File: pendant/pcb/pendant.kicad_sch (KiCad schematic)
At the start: 59 parts, among them CN1 S2B-PH-SM4-TB(LF)(SN), CN2 S4B-PH-SM4-TB(LF)(SN), Q1 DMG3415U-7, SW1 TS-1088-AR02016, SW2 TS-1088-AR02016, U1 ESP32-S3-WROOM-1, U2 TCA8418RTWR, U3 TPS61169DCKR, U5 APX803S-26SA-7, U6 MCP73831T-2ACI/OT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

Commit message: fix errors on pendant pcb
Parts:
- R5: footprint pendant:R0603 -> pendant:R0402; LCSC Part C365454 -> C203098
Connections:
- net DN1 is gone; now on net D-: D3.2, USBC1.A7 (DN1), USBC1.B7 (DN2)
- net VBUSD is gone; now on net VBUS: D4.2, USBC1.A4 (VBUS), USBC1.A9 (VBUS), USBC1.B4 (VBUS), USBC1.B9 (VBUS)
- net 3V3: now also C2.2, L1.2, U3.5 (VIN)
- net AXIS_X: now also U2.12 (COL3); no longer U2.13 (COL4)
- net AXIS_Y: now also U2.13 (COL4); no longer U2.14 (COL5)
- net AXIS_Z: now also U2.14 (COL5); no longer U2.15 (COL6)
- net D+: now also USBC1.A6 (DP1), USBC1.B6 (DP2)
- net D-: no longer D3.1
- net GND: now also D3.1, D4.1, D5.2, U2.19 (GND)
- net SPEED_1: now also U2.15 (COL6); no longer U2.16 (COL7)
- net SPEED_2: now also U2.16 (COL7); no longer U2.17 (COL8)
- net SPEED_3: now also U2.17 (COL8); no longer U2.18 (COL9)
- net SPEED_4: now also U2.18 (COL9); no longer U2.19 (GND)
- net VBUS: no longer C2.2, D4.1, L1.2, U3.5 (VIN)
- removed net DP1: D5.2, USBC1.A6 (DP1), USBC1.B6 (DP2)
- no-connect marks 66 -> 65
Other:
- moved on the sheet: R16

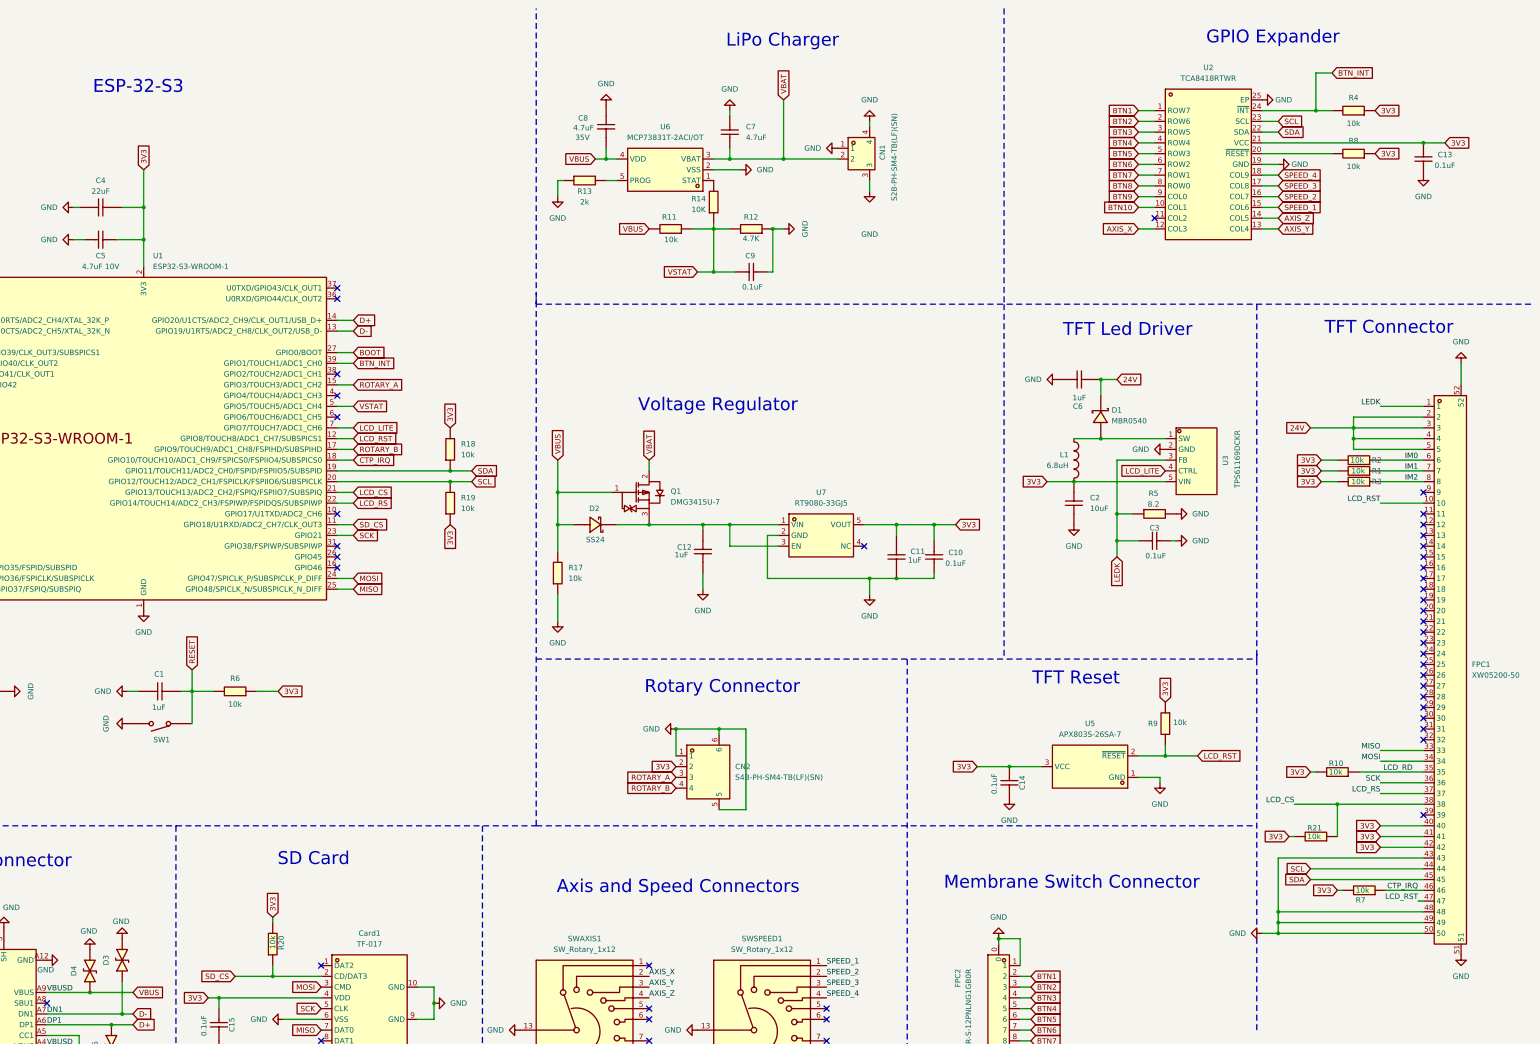
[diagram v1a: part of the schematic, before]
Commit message: update pendant pcb
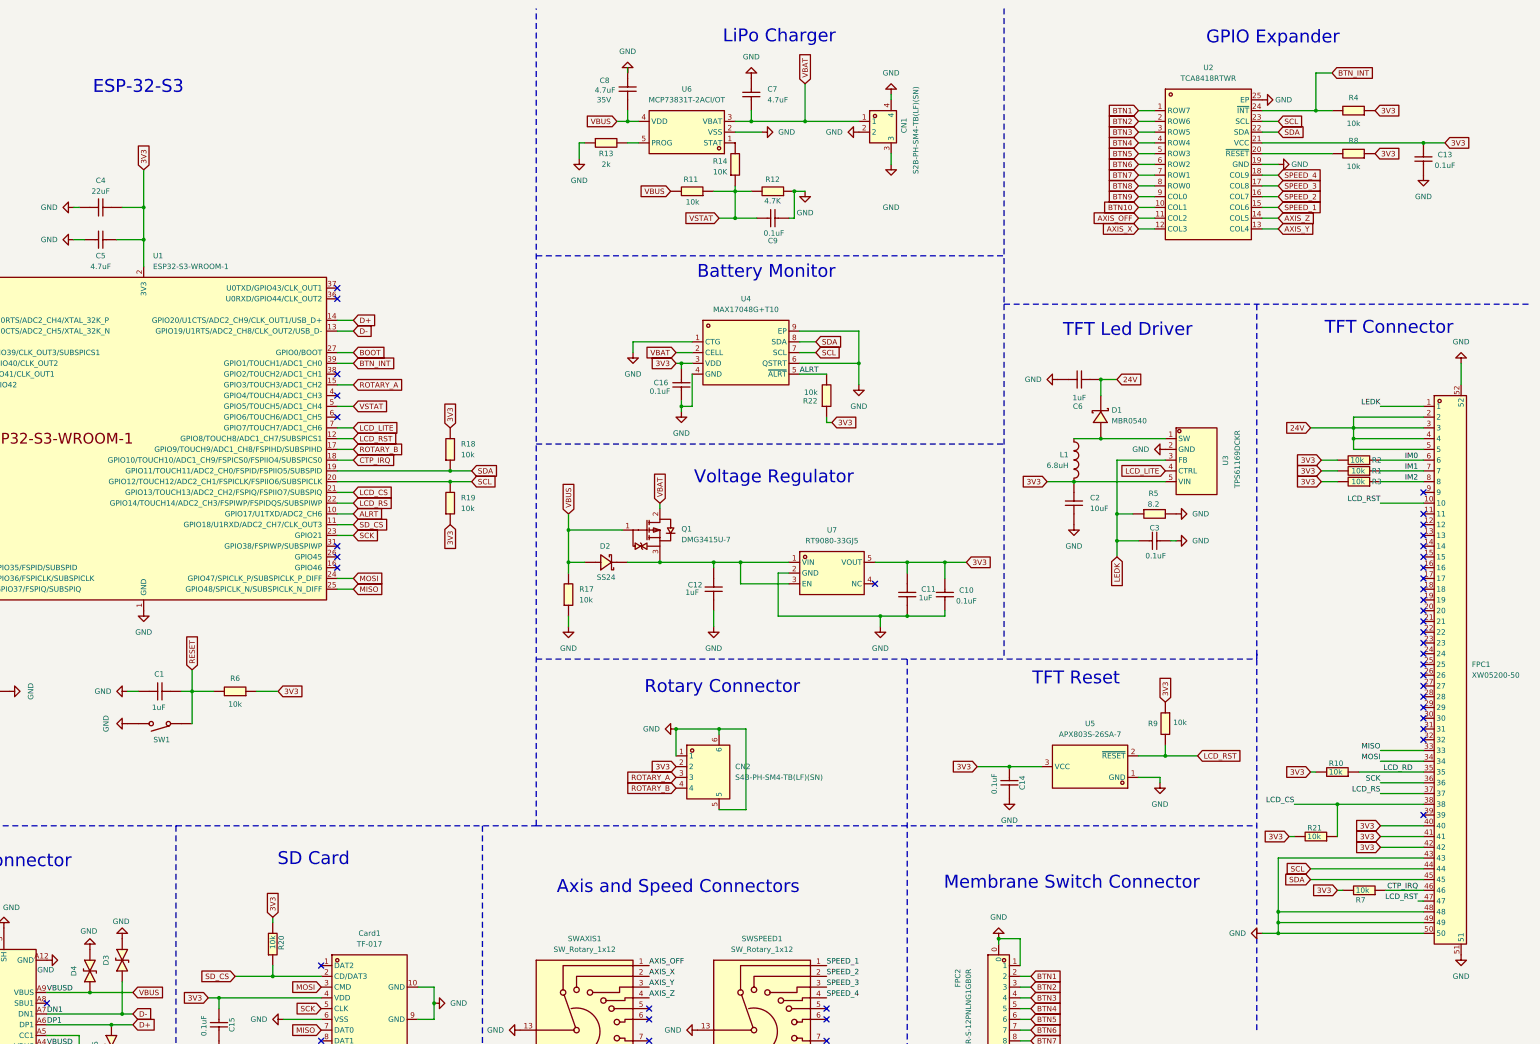
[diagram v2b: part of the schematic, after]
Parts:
- added C16: 0.1uF, pendant:C0402, symbol pendant:CL05B104KO5NNNC
- added R22: 10k, pendant:R0402, symbol pendant:0402WGF1002TCE
- added U4: MAX17048G+T10, pendant:DFN-8_L2.0-W2.0-P0.50-BL-EP, symbol pendant:MAX17048G+T10
- C5: value 4.7uF 10V -> 4.7uF
- SWAXIS1, SWSPEED1: now left out of the parts list
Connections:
- net 3V3: now also C16.1, R22.1, U4.3 (VDD)
- net GND: now also CN1.2, C16.2, U4.1 (CTG), U4.4 (GND), U4.6 (QSTRT), U4.9 (EP); no longer CN1.1
- net SCL: now also U4.7 (SCL)
- net SDA: now also U4.8 (SDA)
- net VBAT: now also CN1.1, U4.2 (CELL); no longer CN1.2
- net AXIS_OFF: now reaches SWAXIS1.1
- net AXIS_OFF: now also U2.11 (COL2)
- net ALRT: now reaches U1.10 (GPIO17/U1TXD/ADC2_CH6)
- net ALRT: now also R22.2, U4.5 (~{ALRT})
- no-connect marks 65 -> 62
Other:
- note added: "Battery Monitor"
- moved on the sheet: C10, C11, C12, C7, C8, C9, D2, Q1, R11, R12, R13, R14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
